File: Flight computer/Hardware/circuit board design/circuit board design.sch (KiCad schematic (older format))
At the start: 0 parts

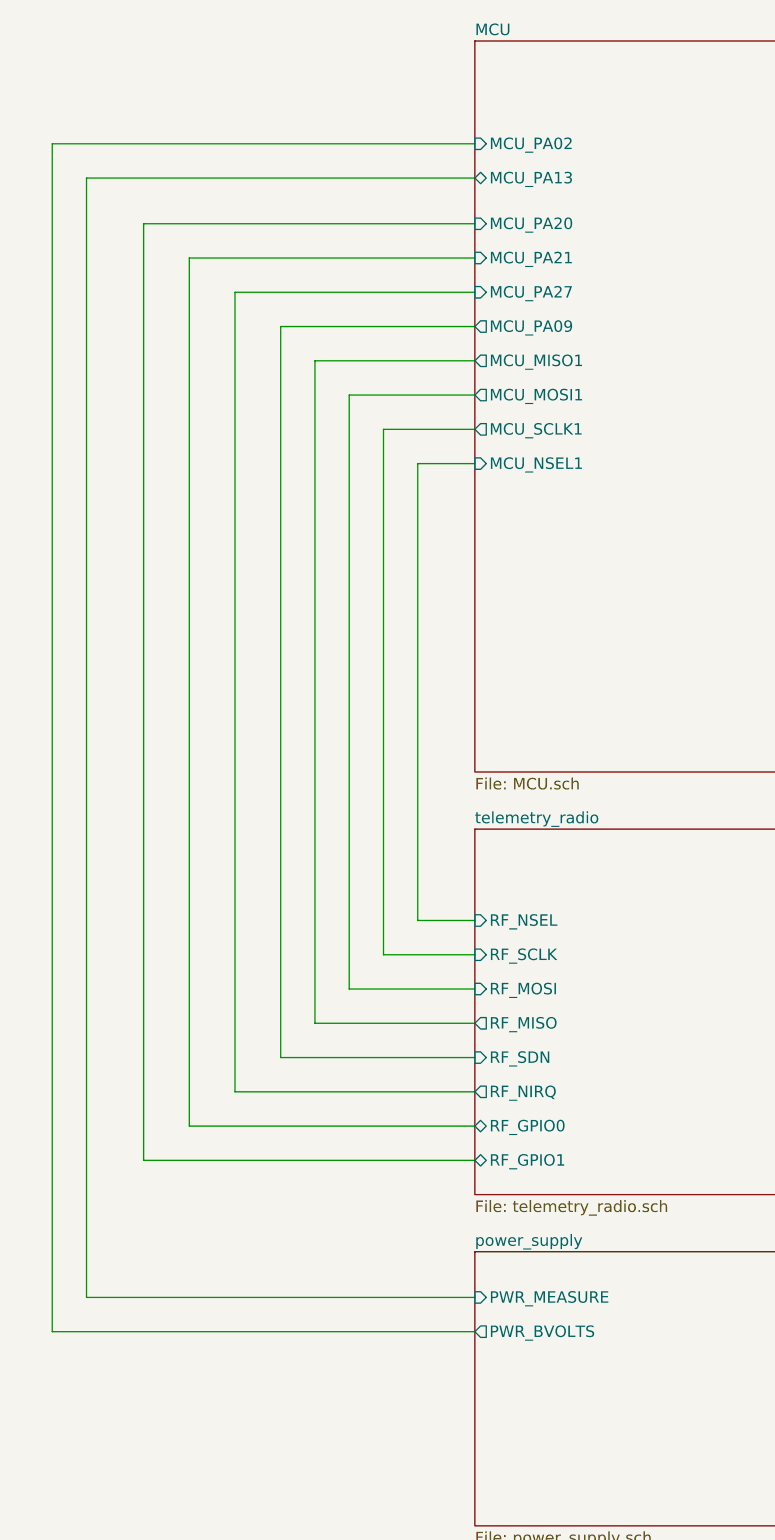
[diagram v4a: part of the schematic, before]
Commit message: moved the USB connector to power_supply schematic
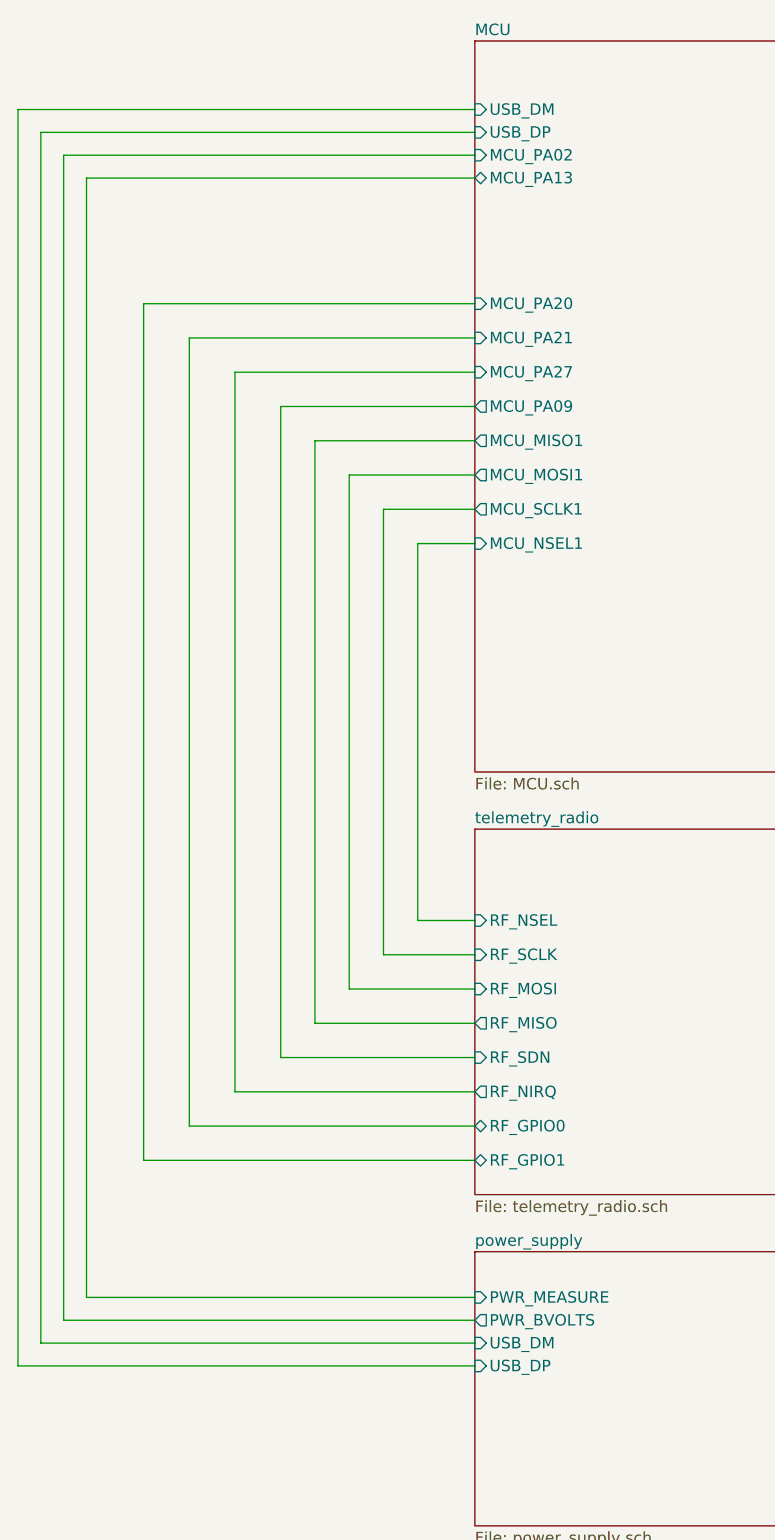
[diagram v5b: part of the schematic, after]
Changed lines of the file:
@@
 Wire Wire Line
 	7900 3900 6950 3900
-$Sheet
-S 2700 6400 2350 1200
-U 5D5B1705
-F0 "power_supply" 50
-F1 "power_supply.sch" 50
-F2 "PWR_BVOLTS" O L 2700 6750 50
-F3 "PWR_MEASURE" I L 2700 6600 50
-$EndSheet
 Wire Wire Line
 	1000 6600 2700 6600
 Wire Wire Line
-	850  6750 2700 6750
-Wire Wire Line
 	1000 1700 1000 6600
-Wire Wire Line
-	850  1550 850  6750
-Wire Wire Line
-	1250 6000 1250 1900
-Wire Wire Line
-	1450 5850 1450 2050
-Wire Wire Line
-	1650 5700 1650 2200
-Wire Wire Line
-	1850 2350 1850 5550
-Wire Wire Line
-	2450 2950 2450 4950
-Wire Wire Line
-	2000 5400 2000 2500
-Wire Wire Line
-	2150 5250 2150 2650
-Wire Wire Line
-	2300 5100 2300 2800
-Wire Wire Line
-	2700 6000 1250 6000
-Wire Wire Line
-	2700 5850 1450 5850
 Wire Wire Line
 	2700 5700 1650 5700
@@
 	7900 4050 6750 4050
 Wire Wire Line
-	1650 2200 2700 2200
-Wire Wire Line
-	1450 2050 2700 2050
-Wire Wire Line
-	1250 1900 2700 1900
-Wire Wire Line
-	7900 2200 5050 2200
-Wire Wire Line
-	5050 1600 7900 1600
-Wire Wire Line
-	5050 2050 7900 2050
-Wire Wire Line
-	2700 1700 1000 1700
-Wire Wire Line
-	1850 2350 2700 2350
-Wire Wire Line
-	6750 2850 5050 2850
-Wire Wire Line
-	6950 2700 5050 2700
-Wire Wire Line
-	2700 1550 850  1550
-Wire Wire Line
-	7900 1300 5050 1300
-Wire Wire Line
-	5050 1450 7900 1450
-Wire Wire Line
-	5050 1900 7150 1900
-Wire Wire Line
-	5050 1750 7350 1750
-Wire Wire Line
-	2000 2500 2700 2500
-Wire Wire Line
-	2700 2950 2450 2950
-Wire Wire Line
-	2300 2800 2700 2800
-Wire Wire Line
-	2150 2650 2700 2650
-$Sheet
-S 2700 1100 2350 3200
-U 5D5B15F7
-F0 "MCU" 50
-F1 "MCU.sch" 50
-F2 "MCU_MOSI1" O L 2700 2650 50
-F3 "MCU_SCLK1" O L 2700 2800 50
-F4 "MCU_NSEL1" I L 2700 2950 50
-F5 "MCU_MISO1" O L 2700 2500 50
-F6 "MCU_SDA3" B R 5050 1750 50
-F7 "MCU_SCL3" B R 5050 1900 50
-F8 "MCU_TXD0" O R 5050 1450 50
-F9 "MCU_RXD0" I R 5050 1300 50
-F10 "MCU_PA02" I L 2700 1550 50
-F11 "MCU_PA05" B R 5050 2700 50
-F12 "MCU_PA06" B R 5050 2850 50
-F13 "MCU_PA07" B R 5050 3000 50
-F14 "MCU_PA09" O L 2700 2350 50
-F15 "MCU_PA13" B L 2700 1700 50
-F16 "MCU_PB03" O R 5050 2050 50
-F17 "MCU_PB02" O R 5050 1600 50
-F18 "MCU_PB08" I R 5050 2200 50
-F19 "MCU_PA20" I L 2700 1900 50
-F20 "MCU_PA21" I L 2700 2050 50
-F21 "MCU_PA27" I L 2700 2200 50
-F22 "MCU_PB04" I R 5050 3250 50
-F23 "MCU_PB05" I R 5050 3350 50
-F24 "MCU_PB13" O R 5050 3700 50
-F25 "MCU_PB14" O R 5050 3800 50
-F26 "MCU_PB06" I R 5050 3450 50
-F27 "MCU_PB07" I R 5050 3550 50
-F28 "MCU_PB15" O R 5050 3900 50
-F29 "MCU_PB16" O R 5050 4000 50
-$EndSheet
-Wire Wire Line
-	5050 3000 6550 3000
-Wire Wire Line
 	6550 3000 6550 4200
 Wire Wire Line
@@
 	6350 5150 6350 3350
 Wire Wire Line
-	6350 3350 5050 3350
-Wire Wire Line
-	5050 3250 6450 3250
-Wire Wire Line
-	5050 3450 6250 3450
-Wire Wire Line
 	6250 3450 6250 5250
 Wire Wire Line
 	6150 5350 6150 3550
 Wire Wire Line
-	6150 3550 5050 3550
-Wire Wire Line
-	5050 3700 6050 3700
-Wire Wire Line
 	6050 3700 6050 5650
 Wire Wire Line
 	5950 5750 5950 3800
 Wire Wire Line
-	5950 3800 5050 3800
-Wire Wire Line
-	5050 3900 5850 3900
-Wire Wire Line
 	5850 3900 5850 5850
 Wire Wire Line
 	5750 5950 5750 4000
-Wire Wire Line
-	5750 4000 5050 4000
 Wire Wire Line
 	7900 5950 5750 5950
@@
 F9 "FIRE_D" O L 7900 5950 50
 $EndSheet
+Wire Wire Line
+	2700 5850 1450 5850
+Wire Wire Line
+	2700 6000 1250 6000
+Wire Wire Line
+	5750 4000 5050 4000
+Wire Wire Line
+	5050 3900 5850 3900
+Wire Wire Line
+	6150 3550 5050 3550
+Wire Wire Line
+	5050 3450 6250 3450
+Wire Wire Line
+	5950 3800 5050 3800
+Wire Wire Line
+	5050 3700 6050 3700
+Wire Wire Line
+	6350 3350 5050 3350
+Wire Wire Line
+	5050 3250 6450 3250
+Wire Wire Line
+	7900 2200 5050 2200
+Wire Wire Line
+	5050 1600 7900 1600
+Wire Wire Line
+	5050 2050 7900 2050
+Wire Wire Line
+	2700 1700 1000 1700
+Wire Wire Line
+	5050 3000 6550 3000
+Wire Wire Line
+	6750 2850 5050 2850
+Wire Wire Line
+	6950 2700 5050 2700
+Wire Wire Line
+	7900 1300 5050 1300
+Wire Wire Line
+	5050 1450 7900 1450
+Wire Wire Line
+	5050 1900 7150 1900
+Wire Wire Line
+	5050 1750 7350 1750
+Wire Wire Line
+	1850 2700 1850 5550
+Wire Wire Line
+	2450 3300 2450 4950
+$Sheet
+S 2700 1100 2350 3200
+U 5D5B15F7
+F0 "MCU" 50
+F1 "MCU.sch" 50
+F2 "MCU_MOSI1" O L 2700 3000 50
+F3 "MCU_SCLK1" O L 2700 3150 50
+F4 "MCU_NSEL1" I L 2700 3300 50
+F5 "MCU_MISO1" O L 2700 2850 50
+F6 "MCU_SDA3" B R 5050 1750 50
+F7 "MCU_SCL3" B R 5050 1900 50
+F8 "MCU_TXD0" O R 5050 1450 50
+F9 "MCU_RXD0" I R 5050 1300 50
+F10 "MCU_PA02" I L 2700 1600 50
+F11 "MCU_PA05" B R 5050 2700 50
+F12 "MCU_PA06" B R 5050 2850 50
+F13 "MCU_PA07" B R 5050 3000 50
+F14 "MCU_PA09" O L 2700 2700 50
+F15 "MCU_PA13" B L 2700 1700 50
+F16 "MCU_PB03" O R 5050 2050 50
+F17 "MCU_PB02" O R 5050 1600 50
+F18 "MCU_PB08" I R 5050 2200 50
+F19 "MCU_PA20" I L 2700 2250 50
+F20 "MCU_PA21" I L 2700 2400 50
+F21 "MCU_PA27" I L 2700 2550 50
+F22 "MCU_PB04" I R 5050 3250 50
+F23 "MCU_PB05" I R 5050 3350 50
+F24 "MCU_PB13" O R 5050 3700 50
+F25 "MCU_PB14" O R 5050 3800 50
+F26 "MCU_PB06" I R 5050 3450 50
+F27 "MCU_PB07" I R 5050 3550 50
+F28 "MCU_PB15" O R 5050 3900 50
+F29 "MCU_PB16" O R 5050 4000 50
+F30 "USB_DP" I L 2700 1500 50
+F31 "USB_DM" I L 2700 1400 50
+$EndSheet
+Wire Wire Line
+	1650 2550 2700 2550
+Wire Wire Line
+	1450 2400 2700 2400
+Wire Wire Line
+	1850 2700 2700 2700
+Wire Wire Line
+	2000 2850 2700 2850
+Wire Wire Line
+	2150 3000 2700 3000
+Wire Wire Line
+	2300 3150 2700 3150
+Wire Wire Line
+	2700 3300 2450 3300
+Wire Wire Line
+	1250 2250 2700 2250
+Wire Wire Line
+	1250 6000 1250 2250
+Wire Wire Line
+	1450 5850 1450 2400
+Wire Wire Line
+	1650 5700 1650 2550
+Wire Wire Line
+	2000 5400 2000 2850
+Wire Wire Line
+	2150 5250 2150 3000
+Wire Wire Line
+	2300 5100 2300 3150
+Wire Wire Line
+	2700 6700 900  6700
+Wire Wire Line
+	900  6700 900  1600
+Wire Wire Line
+	900  1600 2700 1600
+$Sheet
+S 2700 6400 2350 1200
+U 5D5B1705
+F0 "power_supply" 50
+F1 "power_supply.sch" 50
+F2 "PWR_BVOLTS" O L 2700 6700 50
+F3 "PWR_MEASURE" I L 2700 6600 50
+F4 "USB_DM" I L 2700 6800 50
+F5 "USB_DP" I L 2700 6900 50
+$EndSheet
+Wire Wire Line
+	2700 6800 800  6800
+Wire Wire Line
+	800  6800 800  1500
+Wire Wire Line
+	800  1500 2700 1500
+Wire Wire Line
+	2700 1400 700  1400
+Wire Wire Line
+	700  1400 700  6900
+Wire Wire Line
+	700  6900 2700 6900
 $EndSCHEMATC

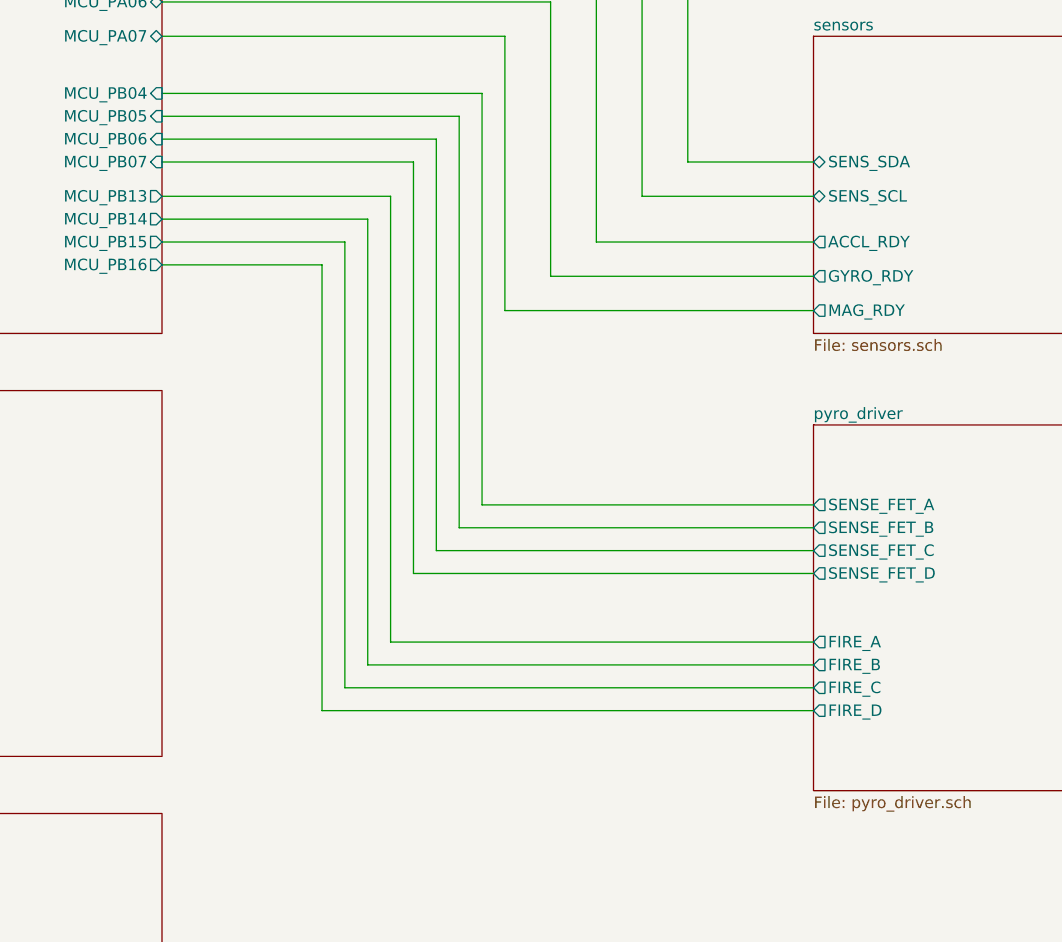
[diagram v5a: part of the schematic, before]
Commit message: added screw terminal symbols and anotated power supply page
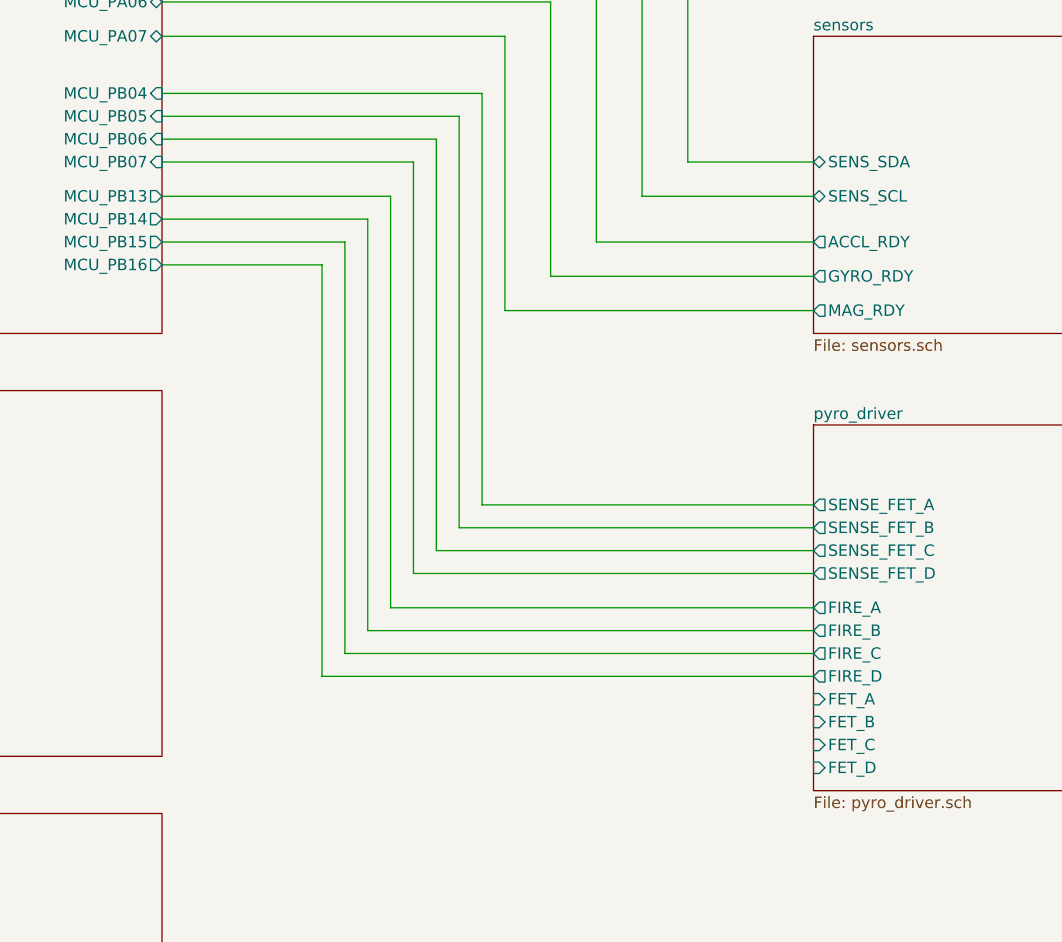
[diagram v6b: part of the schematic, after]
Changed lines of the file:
@@
 	6250 3450 6250 5250
-Wire Wire Line
-	6150 5350 6150 3550
-Wire Wire Line
-	6050 3700 6050 5650
-Wire Wire Line
-	5950 5750 5950 3800
-Wire Wire Line
-	5850 3900 5850 5850
-Wire Wire Line
-	5750 5950 5750 4000
-Wire Wire Line
-	7900 5950 5750 5950
-Wire Wire Line
-	5850 5850 7900 5850
-Wire Wire Line
-	7900 5750 5950 5750
-Wire Wire Line
-	6050 5650 7900 5650
 Wire Wire Line
 	7900 5350 6150 5350
 Wire Wire Line
 	6250 5250 7900 5250
-$Sheet
-S 7900 4700 2350 1600
-U 5D6468D5
-F0 "pyro_driver" 50
-F1 "pyro_driver.sch" 50
-F2 "SENSE_FET_A" O L 7900 5050 50
-F3 "FIRE_A" O L 7900 5650 50
-F4 "SENSE_FET_B" O L 7900 5150 50
-F5 "FIRE_B" O L 7900 5750 50
-F6 "SENSE_FET_C" O L 7900 5250 50
-F7 "FIRE_C" O L 7900 5850 50
-F8 "SENSE_FET_D" O L 7900 5350 50
-F9 "FIRE_D" O L 7900 5950 50
-$EndSheet
 Wire Wire Line
 	2700 5850 1450 5850
@@
 Wire Wire Line
 	5050 3900 5850 3900
-Wire Wire Line
-	6150 3550 5050 3550
-Wire Wire Line
-	5050 3450 6250 3450
 Wire Wire Line
 	5950 3800 5050 3800
@@
 Wire Wire Line
 	700  6900 2700 6900
+Wire Wire Line
+	5050 3450 6250 3450
+$Sheet
+S 7900 4700 2350 1600
+U 5D6468D5
+F0 "pyro_driver" 50
+F1 "pyro_driver.sch" 50
+F2 "SENSE_FET_A" O L 7900 5050 50
+F3 "FIRE_A" O L 7900 5500 50
+F4 "SENSE_FET_B" O L 7900 5150 50
+F5 "FIRE_B" O L 7900 5600 50
+F6 "SENSE_FET_C" O L 7900 5250 50
+F7 "FIRE_C" O L 7900 5700 50
+F8 "SENSE_FET_D" O L 7900 5350 50
+F9 "FIRE_D" O L 7900 5800 50
+F10 "FET_A" I L 7900 5900 50
+F11 "FET_B" I L 7900 6000 50
+F12 "FET_C" I L 7900 6100 50
+F13 "FET_D" I L 7900 6200 50
+$EndSheet
+Wire Wire Line
+	5950 5600 5950 3800
+Wire Wire Line
+	5750 5800 5750 4000
+Wire Wire Line
+	7900 5800 5750 5800
+Wire Wire Line
+	5850 5700 7900 5700
+Wire Wire Line
+	7900 5600 5950 5600
+Wire Wire Line
+	6050 5500 7900 5500
+Wire Wire Line
+	5850 3900 5850 5700
+Wire Wire Line
+	6050 3700 6050 5500
+Wire Wire Line
+	6150 5350 6150 3550
+Wire Wire Line
+	5050 3550 6150 3550
 $EndSCHEMATC

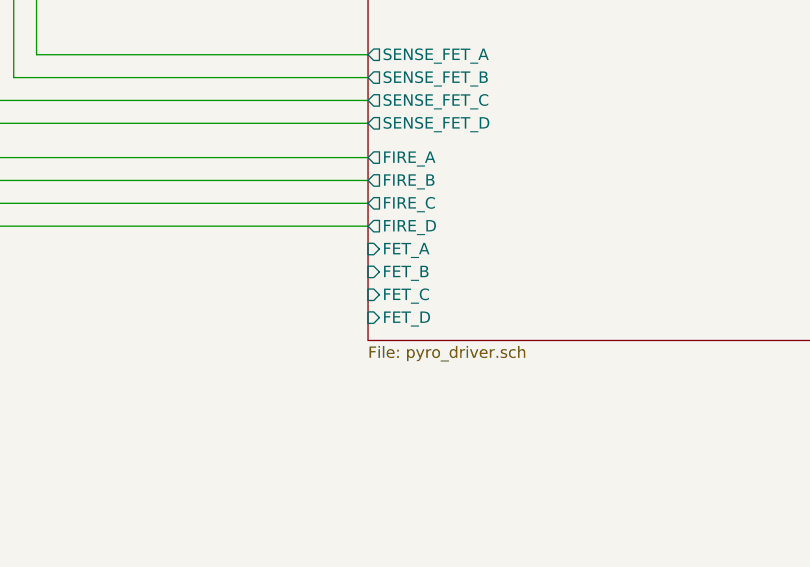
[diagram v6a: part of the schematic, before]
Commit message: set up the PCB to fit formfactor
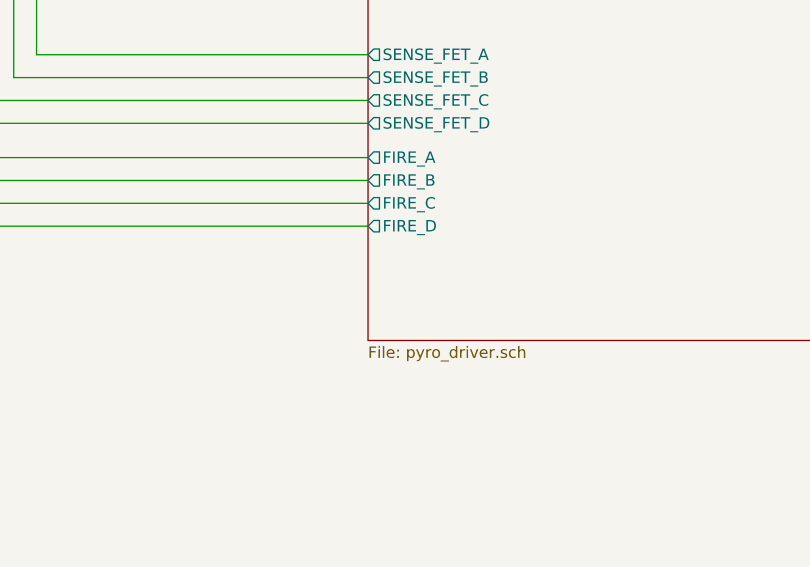
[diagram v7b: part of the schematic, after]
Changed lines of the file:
@@
 F8 "SENSE_FET_D" O L 7900 5350 50
 F9 "FIRE_D" O L 7900 5800 50
-F10 "FET_A" I L 7900 5900 50
-F11 "FET_B" I L 7900 6000 50
-F12 "FET_C" I L 7900 6100 50
-F13 "FET_D" I L 7900 6200 50
 $EndSheet
 Wire Wire Line
